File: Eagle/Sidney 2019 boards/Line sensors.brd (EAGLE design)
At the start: 58.2 x 24.2 mm, 19 parts

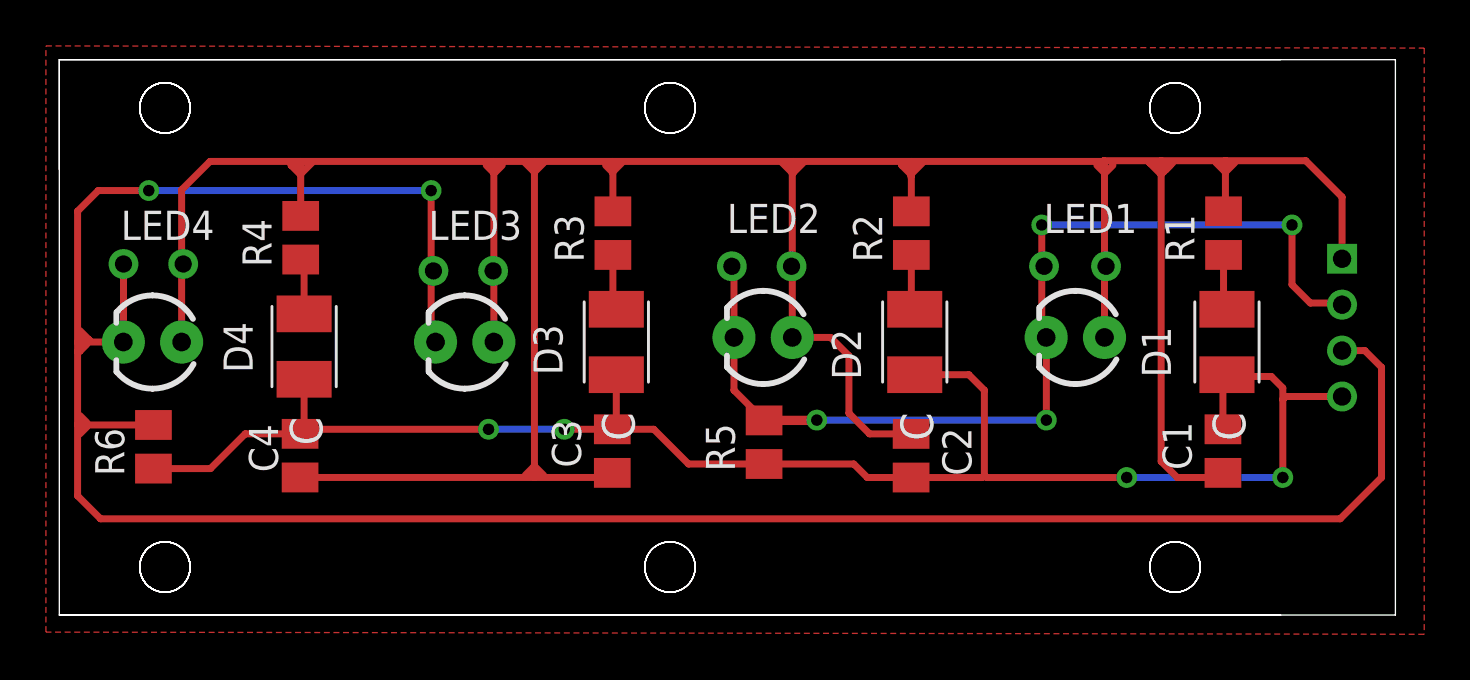
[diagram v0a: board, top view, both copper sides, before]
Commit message: Created DXFs, PDFs and PNGs, small improvements to line sensors board
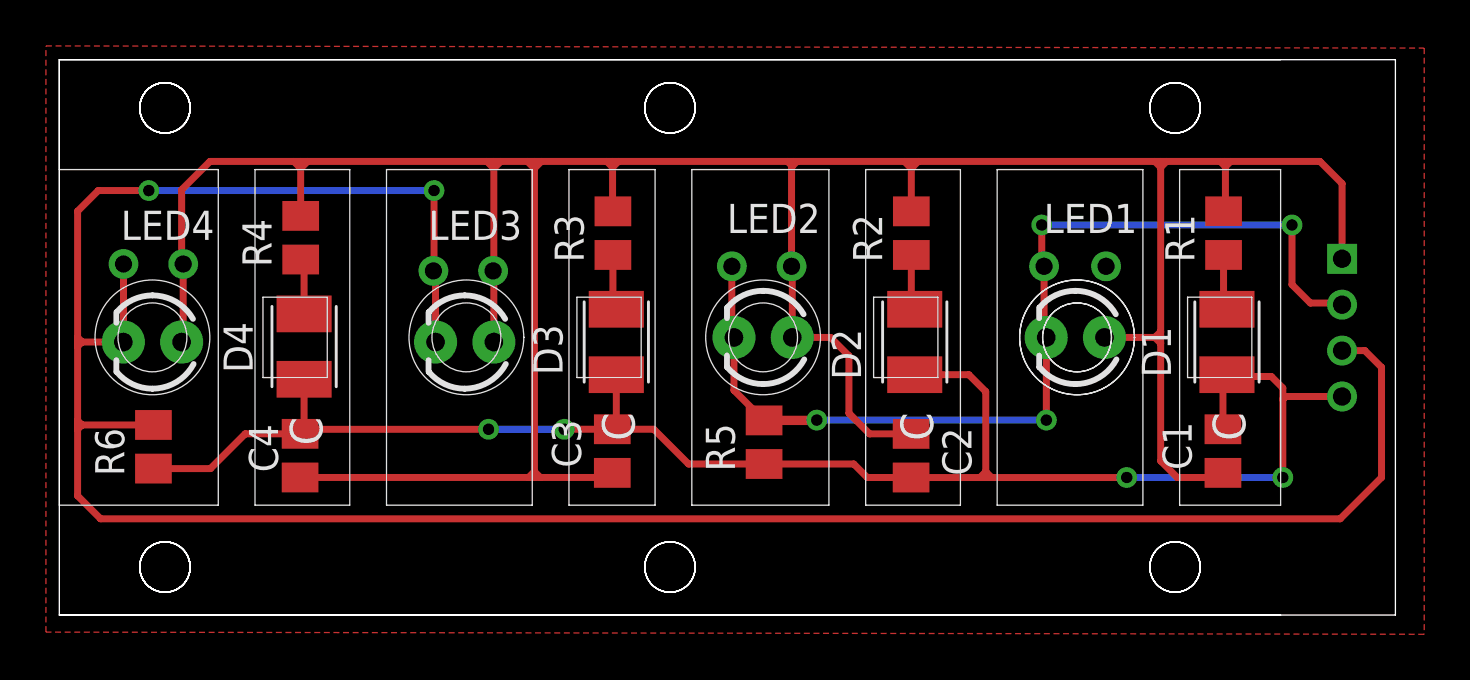
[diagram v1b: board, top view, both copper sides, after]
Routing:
- net SIG2: track 105.5 -> 109.6 mm, vias 2 -> 4
- net N$2: track 3.40 -> 0.00 mm, vias 1 -> 0
- net 5V: track 150.3 -> 148.0 mm, vias 0 -> 3
- net N$35: track 1.77 -> 0.00 mm
- net N$31: track 1.57 -> 0.00 mm
- net N$28: track 1.23 -> 0.00 mm
- net N$27: track 0.99 -> 0.00 mm
- net N$32: track 0.91 -> 0.00 mm
- net GND: track 74.6 -> 75.2 mm
- net N$40: track 0.52 -> 0.00 mm
- net SIG1: track 44.3 -> 44.2 mm, vias 4 -> 6
